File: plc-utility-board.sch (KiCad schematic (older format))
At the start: 0 parts

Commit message: Reorganized everything to use hierarchical sheets in KiCAD. Moved power supply section for motor driver into separate sheet. Moved connectors into top-level sheet
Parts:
- added J1, J11, J9: Screw_Terminal_01x02, symbol Connector:Screw_Terminal_01x02
- added J10, J8: Screw_Terminal_01x03, symbol Connector:Screw_Terminal_01x03
- added J2, J4: Screw_Terminal_01x08, symbol Connector:Screw_Terminal_01x08
- added J3: Screw_Terminal_01x04, symbol Connector:Screw_Terminal_01x04
- added J5: TerminalBlock_02x04, symbol mylib:TerminalBlock_02x04
- added J6, J7: Conn_01x03_Male, symbol Connector:Conn_01x03_Male
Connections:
- new net Motor1 3V3 <- PLC/IN1: J8.1 (Pin_1)
- new net Motor1 3V3 <- PLC/IN2: J8.2 (Pin_2)
- new net Motor1 3V3 <- PLC/IN3: J8.3 (Pin_3)
- new net Motor1 3V3 <- PLC/OUT1: J6.1 (Pin_1)
- new net Motor1 3V3 <- PLC/OUT2: J6.2 (Pin_2)
- new net Motor1 3V3 <- PLC/OUT3: J6.3 (Pin_3)
- new net Motor1 driver/OUTA: J9.1 (Pin_1)
- new net Motor1 driver/OUTB: J9.2 (Pin_2)
- new net Motor2 3V3 <- PLC/IN1: J10.1 (Pin_1)
- new net Motor2 3V3 <- PLC/IN2: J10.2 (Pin_2)
- new net Motor2 3V3 <- PLC/IN3: J10.3 (Pin_3)
- new net Motor2 3V3 <- PLC/OUT1: J7.1 (Pin_1)
- new net Motor2 3V3 <- PLC/OUT2: J7.2 (Pin_2)
- new net Motor2 3V3 <- PLC/OUT3: J7.3 (Pin_3)
- new net Motor2 driver/OUTA: J11.1 (Pin_1)
- new net Motor2 driver/OUTB: J11.2 (Pin_2)
- new net Power section/GND: J1.2 (Pin_2)
- new net Power section/VIN: J1.1 (Pin_1)
- new net plc-to-ttl/IN1: J2.1 (Pin_1)
- new net plc-to-ttl/IN2: J2.2 (Pin_2)
- new net plc-to-ttl/IN3: J2.3 (Pin_3)
- new net plc-to-ttl/IN4: J2.4 (Pin_4)
- new net plc-to-ttl/IN5: J2.5 (Pin_5)
- new net plc-to-ttl/IN6: J2.6 (Pin_6)
- new net plc-to-ttl/IN7: J2.7 (Pin_7)
- new net plc-to-ttl/IN8: J2.8 (Pin_8)
- new net plc-to-ttl/OUT1: J4.1 (Pin_1)
- new net plc-to-ttl/OUT2: J4.2 (Pin_2)
- new net plc-to-ttl/OUT3: J4.3 (Pin_3)
- new net plc-to-ttl/OUT4: J4.4 (Pin_4)
- new net plc-to-ttl/OUT5: J4.5 (Pin_5)
- new net plc-to-ttl/OUT6: J4.6 (Pin_6)
- new net plc-to-ttl/OUT7: J4.7 (Pin_7)
- new net plc-to-ttl/OUT8: J4.8 (Pin_8)
- new net ttl-to-plc/GND: J5.2, J5.4, J5.6, J5.8
- new net ttl-to-plc/IN1: J3.1 (Pin_1)
- new net ttl-to-plc/IN2: J3.2 (Pin_2)
- new net ttl-to-plc/IN3: J3.3 (Pin_3)
- new net ttl-to-plc/IN4: J3.4 (Pin_4)
- new net ttl-to-plc/OUT1: J5.1
- new net ttl-to-plc/OUT2: J5.3
- new net ttl-to-plc/OUT3: J5.5
- new net ttl-to-plc/OUT4: J5.7

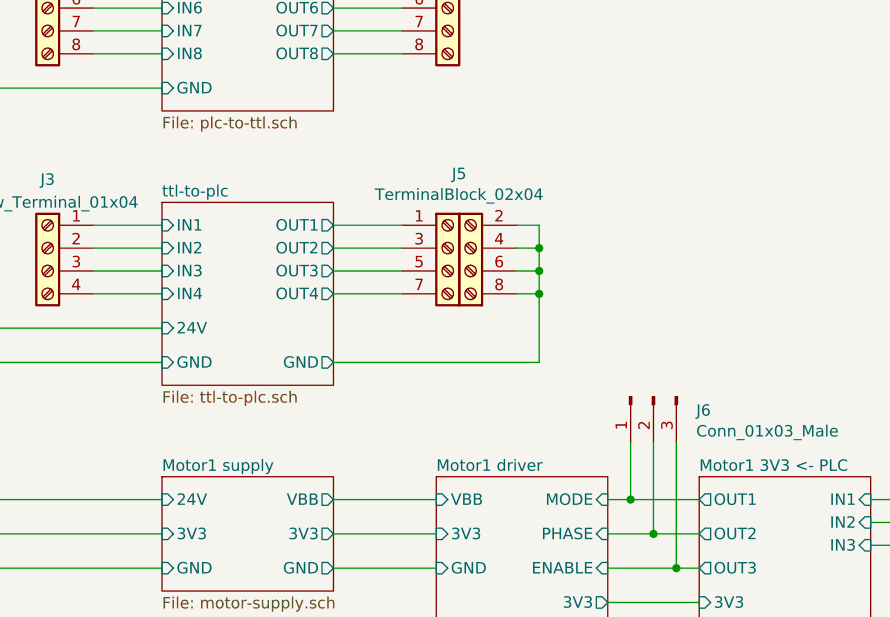
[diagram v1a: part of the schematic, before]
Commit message: Generated annotations, netlists and assigned footprints into components
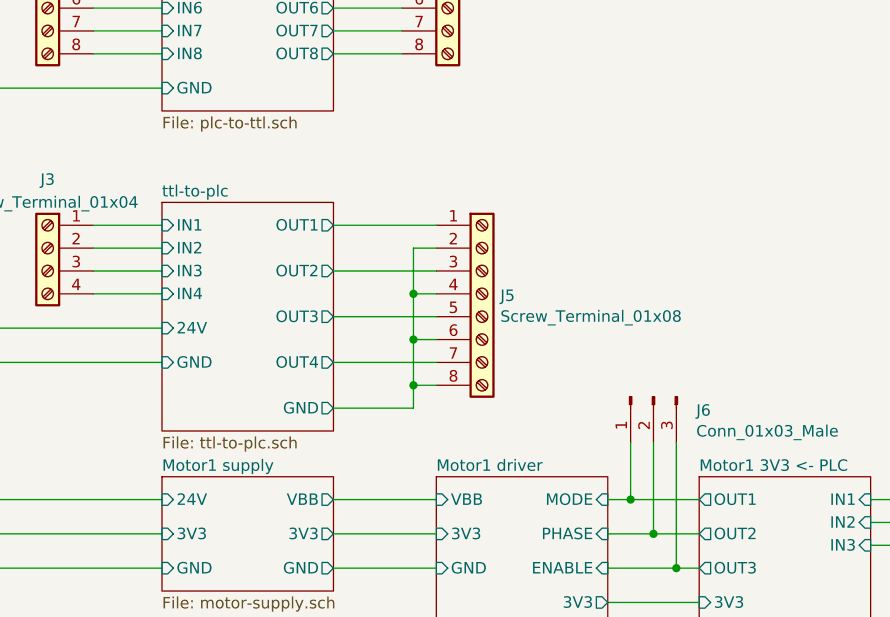
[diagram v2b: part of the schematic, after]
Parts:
- removed J5: TerminalBlock_02x04, symbol mylib:TerminalBlock_02x04
- added J5: Screw_Terminal_01x08, TerminalBlock_Phoenix:TerminalBlock_Phoenix_MKDS-1,5-8-5.08_1x08_P5.08mm_Horizontal, symbol Connector:Screw_Terminal_01x08
- J1: footprint (none) -> TerminalBlock:TerminalBlock_bornier-2_P5.08mm
- J10, J8: footprint (none) -> TerminalBlock_Phoenix:TerminalBlock_Phoenix_MKDS-1,5-3-5.08_1x03_P5.08mm_Horizontal
- J11, J9: footprint (none) -> TerminalBlock_Phoenix:TerminalBlock_Phoenix_MKDS-1,5-2-5.08_1x02_P5.08mm_Horizontal
- J2, J4: footprint (none) -> TerminalBlock_Phoenix:TerminalBlock_Phoenix_MKDS-1,5-8-5.08_1x08_P5.08mm_Horizontal
- J3: footprint (none) -> TerminalBlock_Phoenix:TerminalBlock_Phoenix_MKDS-1,5-4-5.08_1x04_P5.08mm_Horizontal
- J6, J7: footprint (none) -> Connector_PinHeader_2.54mm:PinHeader_1x03_P2.54mm_Vertical
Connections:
- net ttl-to-plc/GND: now also J5.2 (Pin_2), J5.4 (Pin_4), J5.6 (Pin_6), J5.8 (Pin_8)
- net ttl-to-plc/OUT1: now also J5.1 (Pin_1)
- net ttl-to-plc/OUT2: now also J5.3 (Pin_3)
- net ttl-to-plc/OUT3: now also J5.5 (Pin_5)
- net ttl-to-plc/OUT4: now also J5.7 (Pin_7)
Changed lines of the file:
@@
 $EndSheet
 $Sheet
-S 4100 2300 750  800
+S 4100 2300 750  1000
 U 5BDB584C
 F0 "ttl-to-plc" 50
@@
 F2 "24V" I L 4100 2850 50
 F3 "GND" I L 4100 3000 50
-F4 "GND" O R 4850 3000 50
+F4 "GND" O R 4850 3200 50
 F5 "IN1" I L 4100 2400 50
 F6 "IN2" I L 4100 2500 50
@@
 F8 "IN4" I L 4100 2700 50
 F9 "OUT1" O R 4850 2400 50
-F10 "OUT2" O R 4850 2500 50
-F11 "OUT3" O R 4850 2600 50
-F12 "OUT4" O R 4850 2700 50
+F10 "OUT2" O R 4850 2600 50
+F11 "OUT3" O R 4850 2800 50
+F12 "OUT4" O R 4850 3000 50
 $EndSheet
 $Sheet
@@
 F 0 "J8" H 7580 3742 50  0000 L CNN
 F 1 "Screw_Terminal_01x03" H 7580 3651 50  0000 L CNN
-F 2 "" H 7500 3700 50  0001 C CNN
+F 2 "TerminalBlock_Phoenix:TerminalBlock_Phoenix_MKDS-1,5-3-5.08_1x03_P5.08mm_Horizontal" H 7500 3700 50  0001 C CNN
 F 3 "~" H 7500 3700 50  0001 C CNN
 	1    7500 3700
@@
 F 0 "J9" H 7580 4442 50  0000 L CNN
 F 1 "Screw_Terminal_01x02" H 7580 4351 50  0000 L CNN
-F 2 "" H 7500 4450 50  0001 C CNN
+F 2 "TerminalBlock_Phoenix:TerminalBlock_Phoenix_MKDS-1,5-2-5.08_1x02_P5.08mm_Horizontal" H 7500 4450 50  0001 C CNN
 F 3 "~" H 7500 4450 50  0001 C CNN
 	1    7500 4450
@@
 F 0 "J2" H 3600 1750 50  0000 C CNN
 F 1 "Screw_Terminal_01x08" H 3600 1650 50  0000 C CNN
-F 2 "" H 3600 1250 50  0001 C CNN
+F 2 "TerminalBlock_Phoenix:TerminalBlock_Phoenix_MKDS-1,5-8-5.08_1x08_P5.08mm_Horizontal" H 3600 1250 50  0001 C CNN
 F 3 "~" H 3600 1250 50  0001 C CNN
 	1    3600 1250
@@
 F 0 "J4" H 5350 1750 50  0000 C CNN
 F 1 "Screw_Terminal_01x08" H 5350 1650 50  0000 C CNN
-F 2 "" H 5350 1250 50  0001 C CNN
+F 2 "TerminalBlock_Phoenix:TerminalBlock_Phoenix_MKDS-1,5-8-5.08_1x08_P5.08mm_Horizontal" H 5350 1250 50  0001 C CNN
 F 3 "~" H 5350 1250 50  0001 C CNN
 	1    5350 1250
@@
 F 0 "J3" H 3600 2800 50  0000 C CNN
 F 1 "Screw_Terminal_01x04" H 3600 2700 50  0000 C CNN
-F 2 "" H 3600 2500 50  0001 C CNN
+F 2 "TerminalBlock_Phoenix:TerminalBlock_Phoenix_MKDS-1,5-4-5.08_1x04_P5.08mm_Horizontal" H 3600 2500 50  0001 C CNN
 F 3 "~" H 3600 2500 50  0001 C CNN
 	1    3600 2500
@@
 Wire Wire Line
 	3800 2700 4100 2700
-$Comp
-L mylib:TerminalBlock_02x04 J5
-U 1 1 5BF08E3E
-P 5400 2500
-F 0 "J5" H 5400 2825 50  0000 C CNN
-F 1 "TerminalBlock_02x04" H 5400 2734 50  0000 C CNN
-F 2 "" H 5400 2500 50  0001 C CNN
-F 3 "" H 5400 2500 50  0001 C CNN
-	1    5400 2500
-	1    0    0    -1
-$EndComp
-Wire Wire Line
-	4850 2400 5150 2400
-Wire Wire Line
-	4850 2500 5150 2500
-Wire Wire Line
-	4850 2600 5150 2600
-Wire Wire Line
-	4850 2700 5150 2700
-Wire Wire Line
-	4850 3000 5750 3000
-Wire Wire Line
-	5750 3000 5750 2700
-Wire Wire Line
-	5750 2400 5650 2400
-Wire Wire Line
-	5650 2500 5750 2500
-Connection ~ 5750 2500
-Wire Wire Line
-	5750 2500 5750 2400
-Wire Wire Line
-	5650 2600 5750 2600
-Connection ~ 5750 2600
-Wire Wire Line
-	5750 2600 5750 2500
-Connection ~ 5750 2700
-Wire Wire Line
-	5750 2700 5750 2600
-Wire Wire Line
-	5650 2700 5750 2700
 $Sheet
 S 4100 850  750  1050
@@
 F 0 "J1" H 1250 1600 50  0000 C CNN
 F 1 "Screw_Terminal_01x02" H 1250 1300 50  0000 C CNN
-F 2 "" H 1250 1500 50  0001 C CNN
+F 2 "TerminalBlock:TerminalBlock_bornier-2_P5.08mm" H 1250 1500 50  0001 C CNN
 F 3 "~" H 1250 1500 50  0001 C CNN
 	1    1250 1500
@@
 F 0 "J6" V 6310 2963 50  0000 R CNN
 F 1 "Conn_01x03_Male" V 6401 2963 50  0000 R CNN
-F 2 "" H 6250 3150 50  0001 C CNN
+F 2 "Connector_PinHeader_2.54mm:PinHeader_1x03_P2.54mm_Vertical" H 6250 3150 50  0001 C CNN
 F 3 "~" H 6250 3150 50  0001 C CNN
 	1    6250 3150
@@
 F 0 "J10" H 7580 5592 50  0000 L CNN
 F 1 "Screw_Terminal_01x03" H 7580 5501 50  0000 L CNN
-F 2 "" H 7500 5550 50  0001 C CNN
+F 2 "TerminalBlock_Phoenix:TerminalBlock_Phoenix_MKDS-1,5-3-5.08_1x03_P5.08mm_Horizontal" H 7500 5550 50  0001 C CNN
 F 3 "~" H 7500 5550 50  0001 C CNN
 	1    7500 5550
@@
 F 0 "J11" H 7580 6292 50  0000 L CNN
 F 1 "Screw_Terminal_01x02" H 7580 6201 50  0000 L CNN
-F 2 "" H 7500 6300 50  0001 C CNN
+F 2 "TerminalBlock_Phoenix:TerminalBlock_Phoenix_MKDS-1,5-2-5.08_1x02_P5.08mm_Horizontal" H 7500 6300 50  0001 C CNN
 F 3 "~" H 7500 6300 50  0001 C CNN
 	1    7500 6300
@@
 F 0 "J7" V 6310 4813 50  0000 R CNN
 F 1 "Conn_01x03_Male" V 6401 4813 50  0000 R CNN
-F 2 "" H 6250 5000 50  0001 C CNN
+F 2 "Connector_PinHeader_2.54mm:PinHeader_1x03_P2.54mm_Vertical" H 6250 5000 50  0001 C CNN
 F 3 "~" H 6250 5000 50  0001 C CNN
 	1    6250 5000
@@
 Wire Wire Line
 	6250 3350 6250 3750
+$Comp
+L Connector:Screw_Terminal_01x08 J5
+U 1 1 5BDC94A6
+P 5500 2700
+F 0 "J5" H 5580 2692 50  0000 L CNN
+F 1 "Screw_Terminal_01x08" H 5580 2601 50  0000 L CNN
+F 2 "TerminalBlock_Phoenix:TerminalBlock_Phoenix_MKDS-1,5-8-5.08_1x08_P5.08mm_Horizontal" H 5500 2700 50  0001 C CNN
+F 3 "~" H 5500 2700 50  0001 C CNN
+	1    5500 2700
+	1    0    0    -1
+$EndComp
+Wire Wire Line
+	4850 2400 5300 2400
+Wire Wire Line
+	4850 3200 5200 3200
+Wire Wire Line
+	5300 2900 5200 2900
+Wire Wire Line
+	5300 2700 5200 2700
+Wire Wire Line
+	5200 2700 5200 2900
+Connection ~ 5200 2900
+Wire Wire Line
+	5300 2500 5200 2500
+Wire Wire Line
+	5200 2500 5200 2700
+Connection ~ 5200 2700
+Wire Wire Line
+	4850 2600 5300 2600
+Wire Wire Line
+	4850 2800 5300 2800
+Wire Wire Line
+	4850 3000 5300 3000
+Wire Wire Line
+	5200 3100 5300 3100
+Wire Wire Line
+	5200 2900 5200 3100
+Connection ~ 5200 3100
+Wire Wire Line
+	5200 3100 5200 3200
 $EndSCHEMATC

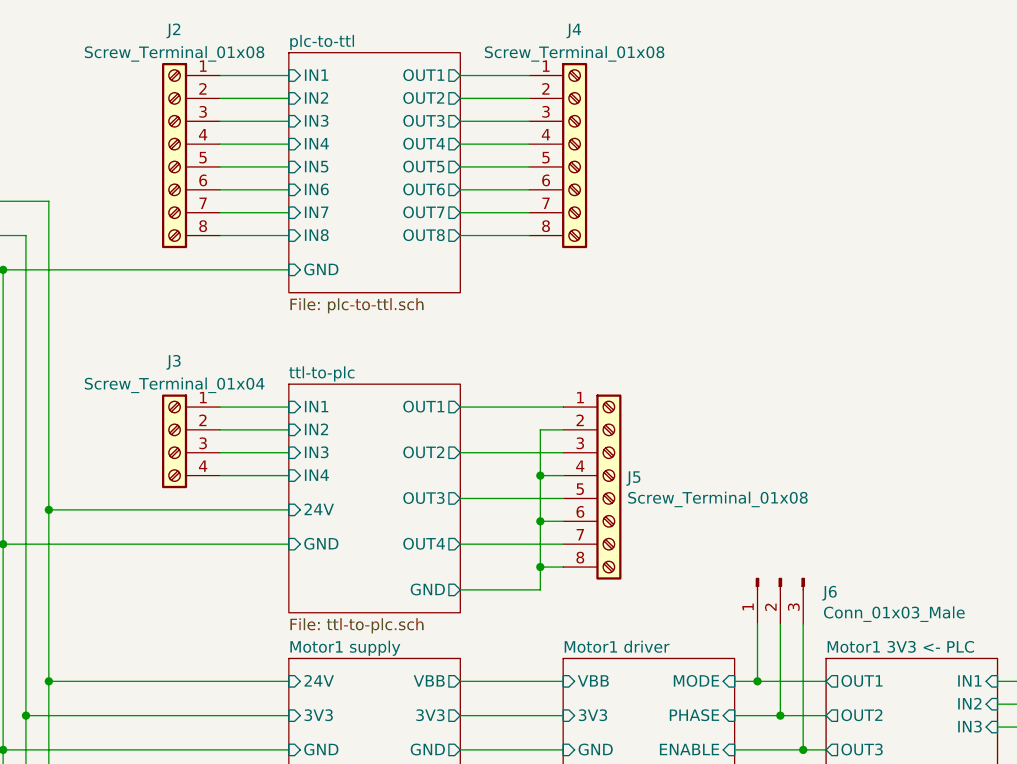
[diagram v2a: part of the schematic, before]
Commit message: Added sketch of PCB. Added circuits for PLC->TTL converter. Modified shape of DG500 component to comply with Phoenix's one
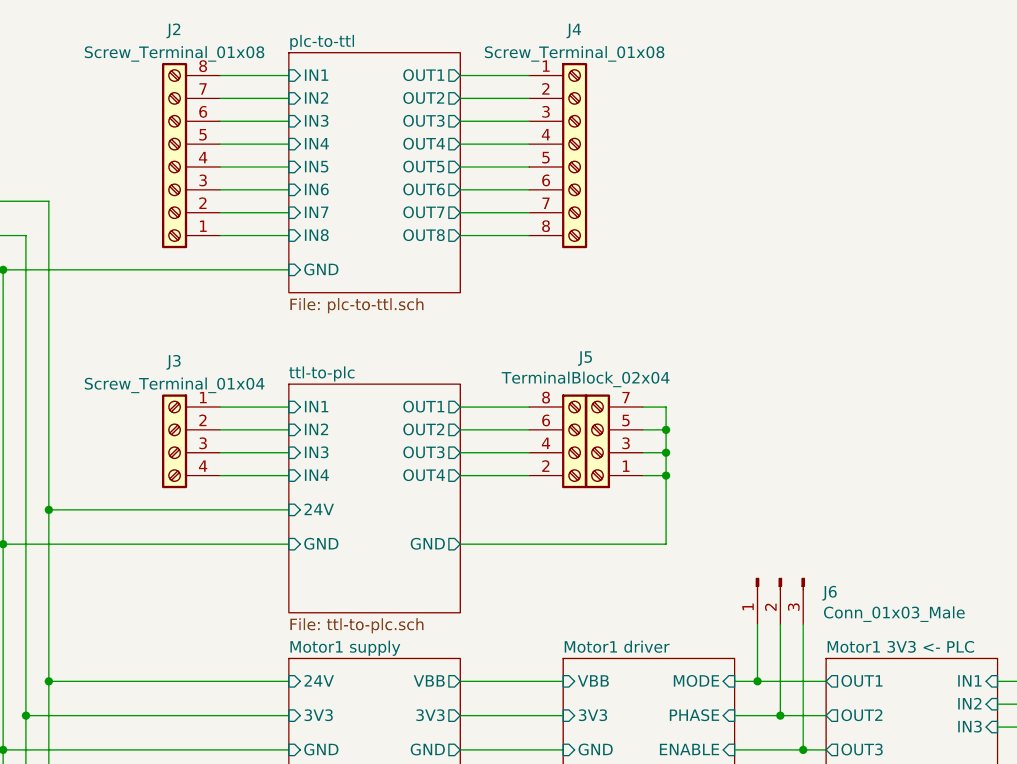
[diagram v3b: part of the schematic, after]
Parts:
- removed J5: Screw_Terminal_01x08, TerminalBlock_Phoenix:TerminalBlock_Phoenix_MKDS-1,5-8-5.08_1x08_P5.08mm_Horizontal, symbol Connector:Screw_Terminal_01x08
- added J5: TerminalBlock_02x04, mylib:DG500B-5.0-4P14, symbol mylib:TerminalBlock_02x04
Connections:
- net plc-to-ttl/IN1: now also J2.8 (Pin_8); no longer J2.1 (Pin_1)
- net plc-to-ttl/IN2: now also J2.7 (Pin_7); no longer J2.2 (Pin_2)
- net plc-to-ttl/IN3: now also J2.6 (Pin_6); no longer J2.3 (Pin_3)
- net plc-to-ttl/IN4: now also J2.5 (Pin_5); no longer J2.4 (Pin_4)
- net plc-to-ttl/IN5: now also J2.4 (Pin_4); no longer J2.5 (Pin_5)
- net plc-to-ttl/IN6: now also J2.3 (Pin_3); no longer J2.6 (Pin_6)
- net plc-to-ttl/IN7: now also J2.2 (Pin_2); no longer J2.7 (Pin_7)
- net plc-to-ttl/IN8: now also J2.1 (Pin_1); no longer J2.8 (Pin_8)
- net ttl-to-plc/GND: now also J5.1, J5.3, J5.5, J5.7
- net ttl-to-plc/OUT1: now also J5.8
- net ttl-to-plc/OUT2: now also J5.6
- net ttl-to-plc/OUT3: now also J5.4
- net ttl-to-plc/OUT4: now also J5.2
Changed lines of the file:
@@
 F2 "24V" I L 4100 2850 50
 F3 "GND" I L 4100 3000 50
-F4 "GND" O R 4850 3200 50
+F4 "GND" O R 4850 3000 50
 F5 "IN1" I L 4100 2400 50
 F6 "IN2" I L 4100 2500 50
@@
 F8 "IN4" I L 4100 2700 50
 F9 "OUT1" O R 4850 2400 50
-F10 "OUT2" O R 4850 2600 50
-F11 "OUT3" O R 4850 2800 50
-F12 "OUT4" O R 4850 3000 50
+F10 "OUT2" O R 4850 2500 50
+F11 "OUT3" O R 4850 2600 50
+F12 "OUT4" O R 4850 2700 50
 $EndSheet
 $Sheet
@@
 L Connector:Screw_Terminal_01x08 J2
 U 1 1 5BE8D7D9
-P 3600 1250
-F 0 "J2" H 3600 1750 50  0000 C CNN
-F 1 "Screw_Terminal_01x08" H 3600 1650 50  0000 C CNN
-F 2 "TerminalBlock_Phoenix:TerminalBlock_Phoenix_MKDS-1,5-8-5.08_1x08_P5.08mm_Horizontal" H 3600 1250 50  0001 C CNN
-F 3 "~" H 3600 1250 50  0001 C CNN
-	1    3600 1250
-	-1   0    0    -1
+P 3600 1350
+F 0 "J2" H 3600 750 50  0000 C CNN
+F 1 "Screw_Terminal_01x08" H 3600 850 50  0000 C CNN
+F 2 "TerminalBlock_Phoenix:TerminalBlock_Phoenix_MKDS-1,5-8-5.08_1x08_P5.08mm_Horizontal" H 3600 1350 50  0001 C CNN
+F 3 "~" H 3600 1350 50  0001 C CNN
+	1    3600 1350
+	-1   0    0    1
 $EndComp
 Wire Wire Line
@@
 Wire Wire Line
 	6250 3350 6250 3750
-$Comp
-L Connector:Screw_Terminal_01x08 J5
-U 1 1 5BDC94A6
-P 5500 2700
-F 0 "J5" H 5580 2692 50  0000 L CNN
-F 1 "Screw_Terminal_01x08" H 5580 2601 50  0000 L CNN
-F 2 "TerminalBlock_Phoenix:TerminalBlock_Phoenix_MKDS-1,5-8-5.08_1x08_P5.08mm_Horizontal" H 5500 2700 50  0001 C CNN
-F 3 "~" H 5500 2700 50  0001 C CNN
-	1    5500 2700
-	1    0    0    -1
-$EndComp
-Wire Wire Line
-	4850 2400 5300 2400
-Wire Wire Line
-	4850 3200 5200 3200
-Wire Wire Line
-	5300 2900 5200 2900
-Wire Wire Line
-	5300 2700 5200 2700
-Wire Wire Line
-	5200 2700 5200 2900
-Connection ~ 5200 2900
-Wire Wire Line
-	5300 2500 5200 2500
-Wire Wire Line
-	5200 2500 5200 2700
-Connection ~ 5200 2700
-Wire Wire Line
-	4850 2600 5300 2600
-Wire Wire Line
-	4850 2800 5300 2800
-Wire Wire Line
-	4850 3000 5300 3000
-Wire Wire Line
-	5200 3100 5300 3100
-Wire Wire Line
-	5200 2900 5200 3100
-Connection ~ 5200 3100
-Wire Wire Line
-	5200 3100 5200 3200
+Wire Wire Line
+	4850 2400 5150 2400
+$Comp
+L mylib:TerminalBlock_02x04 J5
+U 1 1 5BE0B666
+P 5400 2600
+F 0 "J5" H 5400 2183 50  0000 C CNN
+F 1 "TerminalBlock_02x04" H 5400 2274 50  0000 C CNN
+F 2 "mylib:DG500B-5.0-4P14" H 5400 2600 50  0001 C CNN
+F 3 "" H 5400 2600 50  0001 C CNN
+	1    5400 2600
+	-1   0    0    1
+$EndComp
+Wire Wire Line
+	4850 2500 5150 2500
+Wire Wire Line
+	4850 2600 5150 2600
+Wire Wire Line
+	5150 2700 4850 2700
+Wire Wire Line
+	4850 3000 5750 3000
+Wire Wire Line
+	5750 3000 5750 2700
+Wire Wire Line
+	5750 2400 5650 2400
+Wire Wire Line
+	5650 2500 5750 2500
+Connection ~ 5750 2500
+Wire Wire Line
+	5750 2500 5750 2400
+Wire Wire Line
+	5650 2600 5750 2600
+Connection ~ 5750 2600
+Wire Wire Line
+	5750 2600 5750 2500
+Wire Wire Line
+	5650 2700 5750 2700
+Connection ~ 5750 2700
+Wire Wire Line
+	5750 2700 5750 2600
 $EndSCHEMATC
